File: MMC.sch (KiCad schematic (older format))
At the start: 52 parts, among them SW2 SKHHLQA010, SW3 KSS241GLFS, U54 STM32F207VCTx, Y5 XTAL_8MHZ_TXC_7A-8.000MAAE-T

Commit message: 16 warnings, 16 errors
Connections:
- net labels removed: MMC_TRST
- wire segments 183 -> 182
- no-connect marks 21 -> 22
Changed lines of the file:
@@
 	1    0    0    -1
 $EndComp
-Text Label 9600 4000 0    50   ~ 10
-MMC_TRST
-Wire Wire Line
-	10150 4000 8650 4000
 Wire Wire Line
 	7650 7100 7750 7100
@@
 NoConn ~ 6850 6000
 NoConn ~ 6850 6100
+NoConn ~ 8650 4000
+$Comp
+L power:PWR_FLAG #FLG0107
+U 1 1 62BC7CC9
+P 8150 1250
+F 0 "#FLG0107" H 8150 1325 50  0001 C CNN
+F 1 "PWR_FLAG" H 8150 1423 50  0000 C CNN
+F 2 "" H 8150 1250 50  0001 C CNN
+F 3 "" H 8150 1250 50  0001 C CNN
+	1    8150 1250
+	1    0    0    -1
+$EndComp
+$Comp
+L power:PWR_FLAG #FLG0108
+U 1 1 62BDD0EB
+P 6700 2600
+F 0 "#FLG0108" H 6700 2675 50  0001 C CNN
+F 1 "PWR_FLAG" H 6700 2773 50  0000 C CNN
+F 2 "" H 6700 2600 50  0001 C CNN
+F 3 "" H 6700 2600 50  0001 C CNN
+	1    6700 2600
+	1    0    0    -1
+$EndComp
 Wire Bus Line
 	9350 3500 9350 3700

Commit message: shave ERC report down to 5 issues
  * mostly by adding power inputs / outputs to the symbols (many
    power pins were set to bidirectional, which causes issues)
  * remove some stray power symbols which were not connected to
    anything
  * FMC connector: change all VCC and GND pins to Power input type
    (there's a lot of them!!)
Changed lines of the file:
@@
 Text Label 5450 1900 0    50   ~ 10
 ISP_RSTn
-Text HLabel 5200 1900 0    50   Input ~ 10
+Text HLabel 5200 1900 0    50   UnSpc ~ 10
 ISP_RSTn
 Wire Wire Line
@@
 	1    0    0    -1
 $EndComp
+Wire Bus Line
+	1700 4600 1700 5350
+Wire Bus Line
+	9350 3500 9350 3700
 $Comp
 L power:PWR_FLAG #FLG0108
@@
 	1    0    0    -1
 $EndComp
-Wire Bus Line
-	9350 3500 9350 3700
-Wire Bus Line
-	1700 4600 1700 5350
 $EndSCHEMATC

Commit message: I2C voltage translator added, rotated POE bridges, I2C connected to SODIMM, NMOS for power leds indicator, 3V3P connected to SI570 and SODIMM
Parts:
- R138: config (none) -> dnf
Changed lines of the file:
@@
 F 40 "Resistors SMD" H 6400 -2370 60  0001 L CNN "Library Name"
 F 41 "This work is licensed under the Creative Commons CC-BY-SA 4.0 License. To the extent that circuit schematics that use Licensed Material can be considered to be ‘Adapted Material’, then the copyright holder waives article 3.b of the license with respect to these schematics." H 6400 -2460 60  0001 L CNN "License"
+F 42 "dnf" V 6700 1450 50  0000 C CNN "config"
 	1    6400 1350
 	0    1    1    0
@@
 	1    0    0    -1
 $EndComp
-Wire Bus Line
-	1700 4600 1700 5350
-Wire Bus Line
-	9350 3500 9350 3700
 $Comp
 L power:PWR_FLAG #FLG0108
@@
 	1    0    0    -1
 $EndComp
+Wire Bus Line
+	9350 3500 9350 3700
+Wire Bus Line
+	1700 4600 1700 5350
 $EndSCHEMATC

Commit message: More consistent attributes for LEDs and BSS138
Should match Marble-Mini
Fewer complaints from KiBoM
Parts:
- LD11, LD12, LD15: Manufacturer KINGBRIGHT -> WURTH; Part Number 150060VS75000 -> LED_KINGBRIGHT_KPH-1608CGCK
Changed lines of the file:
@@
 F 3 "" H 12450 2840 60  0001 L CNN
 F 4 "Green" H 12450 2750 60  0001 L CNN "Pole4"
-F 5 "150060VS75000" H 12450 2750 60  0001 L CNN "Part Number"
+F 5 "LED_KINGBRIGHT_KPH-1608CGCK" H 12450 2750 60  0001 L CNN "Part Number"
 F 6 "LED Green 1C 2A" H 12450 2660 60  0001 L CNN "Library Ref"
 F 7 "SchLib\\LEDs & Displays.SchLib" H 12450 2570 60  0001 L CNN "Library Path"
@@
 F 14 "~~" H 12450 1850 60  0001 L CNN "Status"
 F 15 "SMD Green LED, Case 1.6mmX0.8mm(0603), 0.65mm Thickness" H 12450 1760 60  0001 L CNN "Part Description"
-F 16 "KINGBRIGHT" H 12450 1670 60  0001 L CNN "Manufacturer"
+F 16 "WURTH" H 12450 1670 60  0001 L CNN "Manufacturer"
 F 17 "150060VS75000" H 12450 1580 60  0001 L CNN "Manufacturer Part Number"
 F 18 "2" H 12450 1490 60  0001 L CNN "Pin Count"
@@
 F 3 "" H 12800 2840 60  0001 L CNN
 F 4 "Green" H 12800 2750 60  0001 L CNN "Pole4"
-F 5 "150060VS75000" H 12800 2750 60  0001 L CNN "Part Number"
+F 5 "LED_KINGBRIGHT_KPH-1608CGCK" H 12800 2750 60  0001 L CNN "Part Number"
 F 6 "LED Green 1C 2A" H 12800 2660 60  0001 L CNN "Library Ref"
 F 7 "SchLib\\LEDs & Displays.SchLib" H 12800 2570 60  0001 L CNN "Library Path"
@@
 F 14 "~~" H 12800 1850 60  0001 L CNN "Status"
 F 15 "SMD Green LED, Case 1.6mmX0.8mm(0603), 0.65mm Thickness" H 12800 1760 60  0001 L CNN "Part Description"
-F 16 "KINGBRIGHT" H 12800 1670 60  0001 L CNN "Manufacturer"
+F 16 "WURTH" H 12800 1670 60  0001 L CNN "Manufacturer"
 F 17 "150060VS75000" H 12800 1580 60  0001 L CNN "Manufacturer Part Number"
 F 18 "2" H 12800 1490 60  0001 L CNN "Pin Count"
@@
 F 3 "" H 13150 2840 60  0001 L CNN
 F 4 "Green" H 13150 2750 60  0001 L CNN "Pole4"
-F 5 "150060VS75000" H 13150 2750 60  0001 L CNN "Part Number"
+F 5 "LED_KINGBRIGHT_KPH-1608CGCK" H 13150 2750 60  0001 L CNN "Part Number"
 F 6 "LED Green 1C 2A" H 13150 2660 60  0001 L CNN "Library Ref"
 F 7 "SchLib\\LEDs & Displays.SchLib" H 13150 2570 60  0001 L CNN "Library Path"
@@
 F 14 "~~" H 13150 1850 60  0001 L CNN "Status"
 F 15 "SMD Green LED, Case 1.6mmX0.8mm(0603), 0.65mm Thickness" H 13150 1760 60  0001 L CNN "Part Description"
-F 16 "KINGBRIGHT" H 13150 1670 60  0001 L CNN "Manufacturer"
+F 16 "WURTH" H 13150 1670 60  0001 L CNN "Manufacturer"
 F 17 "150060VS75000" H 13150 1580 60  0001 L CNN "Manufacturer Part Number"
 F 18 "2" H 13150 1490 60  0001 L CNN "Pin Count"

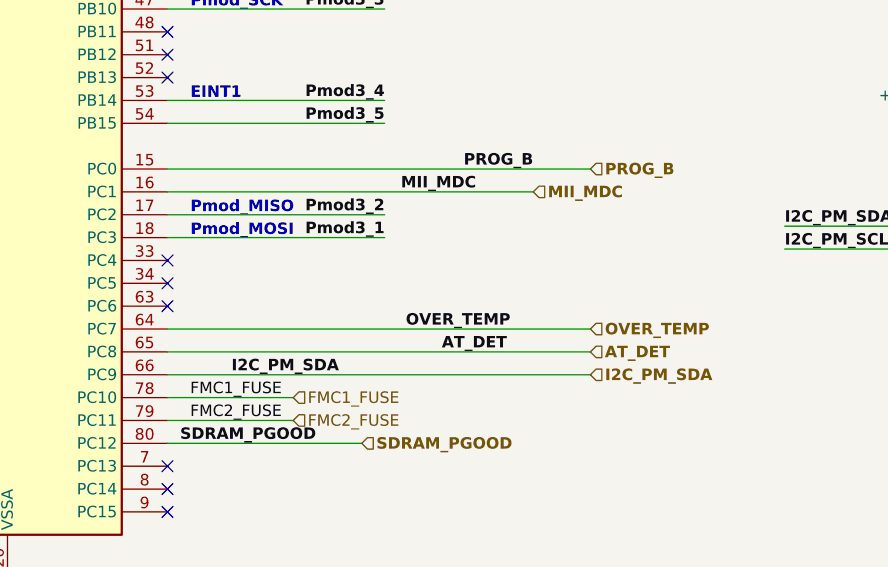
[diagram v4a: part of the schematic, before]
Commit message: reduced reels with components, DDR 1V5 enable signal connected to MMC, DDR I2C pull-ups powerd from 3.3VP
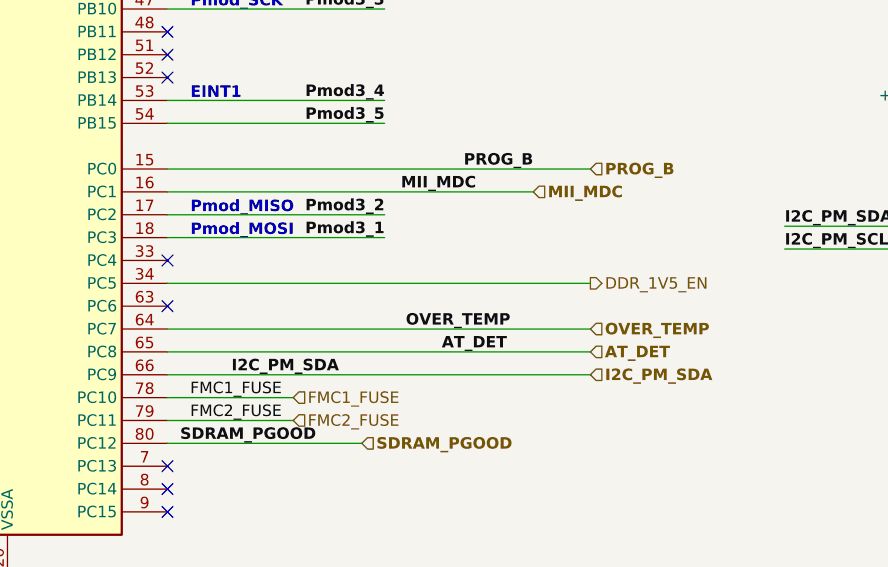
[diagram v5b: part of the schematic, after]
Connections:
- net labels added: DDR_1V5_EN
- wire segments 182 -> 183
- no-connect marks 22 -> 21
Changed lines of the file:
@@
 NoConn ~ 8650 6600
 NoConn ~ 8650 5900
-NoConn ~ 8650 5800
 NoConn ~ 8650 5700
 NoConn ~ 8650 4900
@@
 	1    0    0    -1
 $EndComp
+Text HLabel 10500 5800 2    50   Output ~ 0
+DDR_1V5_EN
+Wire Wire Line
+	10500 5800 8650 5800
 Wire Bus Line
 	9350 3500 9350 3700

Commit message: Flag duplicate generic parts in BOM, and refresh a few cap instances from library to reduce such dups
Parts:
- C102: footprint CAPC1005X55N -> Capacitors SMD:CAPC1005X55N; Comment =Value -> 100pF; ComponentHeight ~~ -> (none); Database Table Name (none) -> Capacitors SMD; Footprint Library (none) -> Capacitors SMD; HelpURL \\\\cern.ch\\dfs\\Applications\\Altium\\Datasheets\\CC0805_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 -> (none); Library Name Capacitors SMD -> Capacitors.DbLib; PackageDescription ~~ -> (none); Pin Count 2.0000000000000000e+00 -> 2; PressFit ~~ -> (none); Sense Comment ~~ -> (none); Status Comment ~~ -> (none)
- C92, C93: HelpURL \\\\cern.ch\\dfs\\Applications\\Altium\\Datasheets\\CC0805_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 -> (none)
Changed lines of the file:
@@
 F 0 "C102" V 2654 3410 50  0000 L CNN
 F 1 "CC0402_100PF_50V_5%_C0G" H 2550 3040 60  0001 L CNN
-F 2 "CAPC1005X55N" H 2550 2230 60  0001 L CNN
-F 3 "\\\\cern.ch\\dfs\\Applications\\Altium\\Datasheets\\CC0805_C0G_KEMET_(Commercial Grade).pdf" H 2550 2860 60  0001 L CNN
+F 2 "Capacitors SMD:CAPC1005X55N" H 2550 2230 60  0001 L CNN
+F 3 " " H 2550 2860 60  0001 L CNN
 F 4 "100pF" V 2745 3410 50  0000 L CNN "~"
 F 5 "CC0402_100PF_50V_5%_C0G" H 2550 2770 60  0001 L CNN "Part Number"
 F 6 "Capacitor - non polarized" H 2550 2680 60  0001 L CNN "Library Ref"
 F 7 "SchLib\\Capacitors.SchLib" H 2550 2590 60  0001 L CNN "Library Path"
-F 8 "=Value" H 2550 2500 60  0001 L CNN "Comment"
+F 8 "100pF" H 2550 2500 60  0001 L CNN "Comment"
 F 9 "Standard" H 2550 2410 60  0001 L CNN "Component Kind"
 F 10 "Standard" H 2550 2320 60  0001 L CNN "Component Type"
-F 11 "2.0000000000000000e+00" H 2550 2140 60  0001 L CNN "Pin Count"
+F 11 "2" H 2550 2140 60  0001 L CNN "Pin Count"
 F 12 "PcbLib\\Capacitors SMD.PcbLib" H 2550 2050 60  0001 L CNN "Footprint Path"
 F 13 "CAPC1005X55N" H 2550 1960 60  0001 L CNN "Footprint Ref"
-F 14 "~~" H 2550 1870 60  0001 L CNN "PackageDescription"
+F 14 " " H 2550 1870 60  0001 L CNN "PackageDescription"
 F 15 "100pF" H 2550 1780 60  0001 L CNN "Val"
 F 16 "Preferred" H 2550 1690 60  0001 L CNN "Status"
-F 17 "~~" H 2550 1600 60  0001 L CNN "Status Comment"
+F 17 " " H 2550 1600 60  0001 L CNN "Status Comment"
 F 18 "50V" H 2550 1510 60  0001 L CNN "Voltage"
 F 19 "C0G/NP0" H 2550 1420 60  0001 L CNN "TC"
@@
 F 26 "No" H 2550 790 60  0001 L CNN "Socket"
 F 27 "Yes" H 2550 700 60  0001 L CNN "SMD"
-F 28 "~~" H 2550 610 60  0001 L CNN "PressFit"
+F 28 " " H 2550 610 60  0001 L CNN "PressFit"
 F 29 "No" H 2550 520 60  0001 L CNN "Sense"
-F 30 "~~" H 2550 430 60  0001 L CNN "Sense Comment"
-F 31 "~~" H 2550 340 60  0001 L CNN "ComponentHeight"
+F 30 " " H 2550 430 60  0001 L CNN "Sense Comment"
+F 31 " " H 2550 340 60  0001 L CNN "ComponentHeight"
 F 32 "KEMET" H 2550 250 60  0001 L CNN "Manufacturer1 Example"
 F 33 "C0402C101J5GACTU" H 2550 160 60  0001 L CNN "Manufacturer1 Part Number"
 F 34 "0.55mm" H 2550 70  60  0001 L CNN "Manufacturer1 ComponentHeight"
-F 35 "\\\\cern.ch\\dfs\\Applications\\Altium\\Datasheets\\CC0805_C0G_KEMET_(Commercial Grade).pdf" H 2550 -20 60  0001 L CNN "HelpURL"
-F 36 "CERN DEM JLC" H 2550 -110 60  0001 L CNN "Author"
-F 37 "12/03/07 00:00:00" H 2550 -200 60  0001 L CNN "CreateDate"
-F 38 "04/22/15 00:00:00" H 2550 -290 60  0001 L CNN "LatestRevisionDate"
-F 39 "Capacitors SMD" H 2550 -380 60  0001 L CNN "Library Name"
-F 40 "This work is licensed under the Creative Commons CC-BY-SA 4.0 License. To the extent that circuit schematics that use Licensed Material can be considered to be ‘Adapted Material’, then the copyright holder waives article 3.b of the license with respect to these schematics." H 2550 -470 60  0001 L CNN "License"
+F 35 "CERN DEM JLC" H 2550 -110 60  0001 L CNN "Author"
+F 36 "12/03/07 00:00:00" H 2550 -200 60  0001 L CNN "CreateDate"
+F 37 "04/22/15 00:00:00" H 2550 -290 60  0001 L CNN "LatestRevisionDate"
+F 38 "Capacitors.DbLib" H 2550 -380 60  0001 L CNN "Library Name"
+F 39 "This work is licensed under the Creative Commons CC-BY-SA 4.0 License. To the extent that circuit schematics that use Licensed Material can be considered to be ‘Adapted Material’, then the copyright holder waives article 3.b of the license with respect to these schematics." H 2550 -470 60  0001 L CNN "License"
+F 40 "Capacitors SMD" H 2550 3300 50  0001 C CNN "Database Table Name"
+F 41 "Capacitors SMD" H 2550 3300 50  0001 C CNN "Footprint Library"
 	1    2550 3300
 	0    1    1    0
@@
 F 1 "CC0402_22PF_50V_5%_C0G" H 2000 3090 60  0001 L CNN
 F 2 "CAPC1005X55N" H 2000 2280 60  0001 L CNN
-F 3 "\\\\cern.ch\\dfs\\Applications\\Altium\\Datasheets\\CC0805_C0G_KEMET_(Commercial Grade).pdf" H 2000 2910 60  0001 L CNN
+F 3 " " H 2000 2910 60  0001 L CNN
 F 4 "22pF" V 2195 3460 50  0000 L CNN "~"
 F 5 "CC0402_22PF_50V_5%_C0G" H 2000 2820 60  0001 L CNN "Part Number"
@@
 F 33 "C0402C220J5GACTU" H 2000 210 60  0001 L CNN "Manufacturer1 Part Number"
 F 34 "0.55mm" H 2000 120 60  0001 L CNN "Manufacturer1 ComponentHeight"
-F 35 "\\\\cern.ch\\dfs\\Applications\\Altium\\Datasheets\\CC0805_C0G_KEMET_(Commercial Grade).pdf" H 2000 30  60  0001 L CNN "HelpURL"
-F 36 "CERN DEM JLC" H 2000 -60 60  0001 L CNN "Author"
-F 37 "12/03/07 00:00:00" H 2000 -150 60  0001 L CNN "CreateDate"
-F 38 "12/03/07 00:00:00" H 2000 -240 60  0001 L CNN "LatestRevisionDate"
-F 39 "Capacitors SMD" H 2000 -330 60  0001 L CNN "Library Name"
-F 40 "This work is licensed under the Creative Commons CC-BY-SA 4.0 License. To the extent that circuit schematics that use Licensed Material can be considered to be ‘Adapted Material’, then the copyright holder waives article 3.b of the license with respect to these schematics." H 2000 -420 60  0001 L CNN "License"
-F 41 "dnf" V 2300 3550 50  0000 C CNN "config"
+F 35 "CERN DEM JLC" H 2000 -60 60  0001 L CNN "Author"
+F 36 "12/03/07 00:00:00" H 2000 -150 60  0001 L CNN "CreateDate"
+F 37 "12/03/07 00:00:00" H 2000 -240 60  0001 L CNN "LatestRevisionDate"
+F 38 "Capacitors SMD" H 2000 -330 60  0001 L CNN "Library Name"
+F 39 "This work is licensed under the Creative Commons CC-BY-SA 4.0 License. To the extent that circuit schematics that use Licensed Material can be considered to be ‘Adapted Material’, then the copyright holder waives article 3.b of the license with respect to these schematics." H 2000 -420 60  0001 L CNN "License"
+F 40 "dnf" V 2300 3550 50  0000 C CNN "config"
 	1    2000 3350
 	0    1    1    0
@@
 F 33 "C0402C151J5GACTU" H 1500 210 60  0001 L CNN "Manufacturer1 Part Number"
 F 34 "0.55mm" H 1500 120 60  0001 L CNN "Manufacturer1 ComponentHeight"
-F 35 "\\\\cern.ch\\dfs\\Applications\\Altium\\Datasheets\\CC0805_C0G_KEMET_(Commercial Grade).pdf" H 1500 30  60  0001 L CNN "HelpURL"
-F 36 "CERN DEM JLC" H 1500 -60 60  0001 L CNN "Author"
-F 37 "12/03/07 00:00:00" H 1500 -150 60  0001 L CNN "CreateDate"
-F 38 "04/22/15 00:00:00" H 1500 -240 60  0001 L CNN "LatestRevisionDate"
-F 39 "Capacitors SMD" H 1500 -330 60  0001 L CNN "Library Name"
-F 40 "This work is licensed under the Creative Commons CC-BY-SA 4.0 License. To the extent that circuit schematics that use Licensed Material can be considered to be ‘Adapted Material’, then the copyright holder waives article 3.b of the license with respect to these schematics." H 1500 -420 60  0001 L CNN "License"
+F 35 "CERN DEM JLC" H 1500 -60 60  0001 L CNN "Author"
+F 36 "12/03/07 00:00:00" H 1500 -150 60  0001 L CNN "CreateDate"
+F 37 "04/22/15 00:00:00" H 1500 -240 60  0001 L CNN "LatestRevisionDate"
+F 38 "Capacitors SMD" H 1500 -330 60  0001 L CNN "Library Name"
+F 39 "This work is licensed under the Creative Commons CC-BY-SA 4.0 License. To the extent that circuit schematics that use Licensed Material can be considered to be ‘Adapted Material’, then the copyright holder waives article 3.b of the license with respect to these schematics." H 1500 -420 60  0001 L CNN "License"
 	1    1500 3350
 	0    1    1    0

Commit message: Progress on the BOM
Fill in many Manufacturer fields
Move dnf flag from Y1 to Y2
Manufacturer Part Number changes for Y1 D8 J6 J9
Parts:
- SW3: footprint AG5300_2:KSS241GLFS -> Marble:KSS241GLFS; Manufacturer (none) -> C&K
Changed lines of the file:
@@
 F 0 "SW3" H 11950 2100 50  0000 C CNN
 F 1 "KSS241GLFS" H 11950 2094 50  0001 C CNN
-F 2 "AG5300_2:KSS241GLFS" H 11950 2100 50  0001 C CNN
+F 2 "Marble:KSS241GLFS" H 11950 2100 50  0001 C CNN
 F 3 "KSS241GLFS" H 11950 2100 50  0001 C CNN
 F 4 "KSS241GLFS" H 11950 1900 50  0001 C CNN "Manufacturer Part Number"
+F 5 "C&K" H 11950 1900 50  0001 C CNN "Manufacturer"
 	1    11950 1900
 	-1   0    0    -1

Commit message: More progress on the BOM
Fill in more Manufacturer and Manufacturer Part Number
Manufacturer Part Number changes for D6 D7
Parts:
- SW2: Manufacturer (none) -> ALPS
- U54: Manufacturer (none) -> ST MICROELECTRONICS; Manufacturer Part Number (none) -> STM32F207VCT6
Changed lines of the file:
@@
 F 4 "SKHHLQA010" H 11950 1500 50  0001 C CNN "Manufacturer Part Number"
 F 5 "dnf" H 11950 1450 50  0000 C CNN "confing"
+F 6 "ALPS" H 11950 1500 50  0001 C CNN "Manufacturer"
 	1    11950 1500
 	-1   0    0    -1
@@
 F 2 "Package_QFP:LQFP-100_14x14mm_P0.5mm" H 7050 1700 50  0001 R CNN
 F 3 "http://www.st.com/st-web-ui/static/active/en/resource/technical/document/datasheet/CD00237391.pdf" H 7750 4300 50  0001 C CNN
+F 4 "ST MICROELECTRONICS" H 7750 4300 50  0001 C CNN "Manufacturer"
+F 5 "STM32F207VCT6" H 7750 4300 50  0001 C CNN "Manufacturer Part Number"
 	1    7750 4300
 	1    0    0    -1
